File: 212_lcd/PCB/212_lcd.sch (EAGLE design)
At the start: 18 parts

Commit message: change 212 parts
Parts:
- Q1: device FaBo-etc:NPN-SMD -> FaBo-Parts:NPN-SMD
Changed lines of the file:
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@@
 <part name="R5" library="FaBo-Resistors" deviceset="RESISTOR" device="-0603" value="10k"/>
 <part name="R6" library="FaBo-Resistors" deviceset="RESISTOR" device="-0603" value="10k"/>
-<part name="Q1" library="FaBo-etc" deviceset="NPN" device="-SMD"/>
 <part name="C1" library="FaBo-Capacitor" deviceset="CAPACITOR" device="-0603" value="0.1uF"/>
 <part name="5V1" library="FaBo-Supply" deviceset="5V" device=""/>
@@
 <part name="GND9" library="FaBo-Supply" deviceset="GND" device=""/>
 <part name="U$2" library="FaBo-etc" deviceset="LOGO_OSHW" device="-M_BOTTOM"/>
+<part name="Q1" library="FaBo-Parts" deviceset="NPN" device="-SMD"/>
 </parts>
 <sheets>
@@
 <instance part="R5" gate="G$1" x="205.74" y="127" rot="R90"/>
 <instance part="R6" gate="G$1" x="228.6" y="127" rot="R90"/>
-<instance part="Q1" gate="G$1" x="134.62" y="142.24"/>
 <instance part="C1" gate="G$1" x="99.06" y="53.34" rot="R90"/>
 <instance part="5V1" gate="G$1" x="38.1" y="160.02"/>
@@
 <instance part="GND9" gate="G$1" x="134.62" y="45.72"/>
 <instance part="U$2" gate="G$1" x="248.92" y="12.7"/>
+<instance part="Q1" gate="G$1" x="134.62" y="142.24"/>
 </instances>
 <busses>
@@
 <segment>
 <wire x1="137.16" y1="137.16" x2="137.16" y2="129.54" width="0.1524" layer="91"/>
+<pinref part="GND3" gate="G$1" pin="GND"/>
 <pinref part="Q1" gate="G$1" pin="E"/>
-<pinref part="GND3" gate="G$1" pin="GND"/>
-</segment>
-<segment>
+</segment>
+<segment>

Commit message: change 212 i2c pull-up
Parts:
- J1: device FaBo-Template:FABO_BRICK_I2C-S04B-PASK-2 -> FaBo-Template:FABO_BRICK_I2C-S04B-PASK-2_LONG
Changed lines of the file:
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@@
 <setting verticaltext="up"/>
 </settings>
-<grid distance="0.1" unitdist="inch" unit="inch" style="lines" multiple="1" display="yes" altdistance="0.01" altunitdist="inch" altunit="inch"/>
+<grid distance="0.1" unitdist="inch" unit="inch" style="lines" multiple="1" display="no" altdistance="0.01" altunitdist="inch" altunit="inch"/>
 <layers>
 <layer number="1" name="Top" color="4" fill="1" visible="no" active="no"/>
@@
 <part name="U$4" library="FaBo-etc" deviceset="SCREW-PAD" device="-3MM"/>
 <part name="U$5" library="FaBo-etc" deviceset="SCREW-PAD" device="-3MM"/>
-<part name="J1" library="FaBo-Template" deviceset="FABO_BRICK_I2C" device="-S04B-PASK-2"/>
 <part name="CN1" library="FaBo-PIN" deviceset="PIN_HEADER_1X16" device="-LONG"/>
 <part name="SJ1" library="FaBo-Supply" deviceset="SMD-JUMPER-2" device="-OPEN" value="OPEN"/>
@@
 <part name="U$2" library="FaBo-etc" deviceset="LOGO_OSHW" device="-M_BOTTOM"/>
 <part name="Q1" library="FaBo-Parts" deviceset="NPN" device="-SMD"/>
+<part name="J1" library="FaBo-Template" deviceset="FABO_BRICK_I2C" device="-S04B-PASK-2_LONG"/>
 </parts>
 <sheets>
@@
 <instance part="U$4" gate="G$1" x="157.48" y="7.62"/>
 <instance part="U$5" gate="G$1" x="149.86" y="7.62"/>
-<instance part="J1" gate="G$1" x="25.4" y="142.24"/>
 <instance part="CN1" gate="G$1" x="15.24" y="63.5" rot="R270"/>
 <instance part="SJ1" gate="G$1" x="182.88" y="144.78"/>
@@
 <instance part="U$2" gate="G$1" x="248.92" y="12.7"/>
 <instance part="Q1" gate="G$1" x="134.62" y="142.24"/>
+<instance part="J1" gate="G$1" x="25.4" y="142.24"/>
 </instances>
 <busses>
@@
 <wire x1="38.1" y1="160.02" x2="38.1" y2="139.7" width="0.1524" layer="91"/>
 <wire x1="38.1" y1="139.7" x2="33.02" y2="139.7" width="0.1524" layer="91"/>
+<pinref part="5V1" gate="G$1" pin="5V"/>
 <pinref part="J1" gate="G$1" pin="VCC"/>
-<pinref part="5V1" gate="G$1" pin="5V"/>
 </segment>
 <segment>
@@
 <wire x1="33.02" y1="134.62" x2="38.1" y2="134.62" width="0.1524" layer="91"/>
 <wire x1="38.1" y1="134.62" x2="38.1" y2="129.54" width="0.1524" layer="91"/>
+<pinref part="GND1" gate="G$1" pin="GND"/>
 <pinref part="J1" gate="G$1" pin="GND"/>
-<pinref part="GND1" gate="G$1" pin="GND"/>
-</segment>
-<segment>
+</segment>
+<segment>

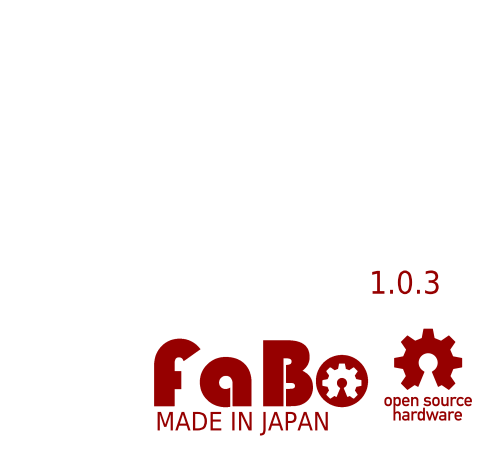
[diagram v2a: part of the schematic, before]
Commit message: change 212 packages
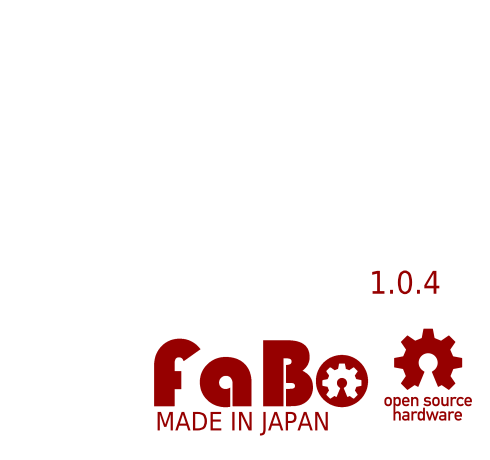
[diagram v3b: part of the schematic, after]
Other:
- note added: "1.0.4"
- note removed: "1.0.3"
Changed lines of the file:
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@@
 <sheet>
 <plain>
-<text x="246.38" y="20.32" size="2.54" layer="94" align="bottom-center">1.0.3</text>
+<text x="246.38" y="20.32" size="2.54" layer="94" align="bottom-center">1.0.4</text>
 </plain>
 <instances>
